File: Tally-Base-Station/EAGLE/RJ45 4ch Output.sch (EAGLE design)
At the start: 9 parts, among them J1 CAMOUT1, J2 CAMOUT2, J3 CAMOUT3, J4 CAMOUT4

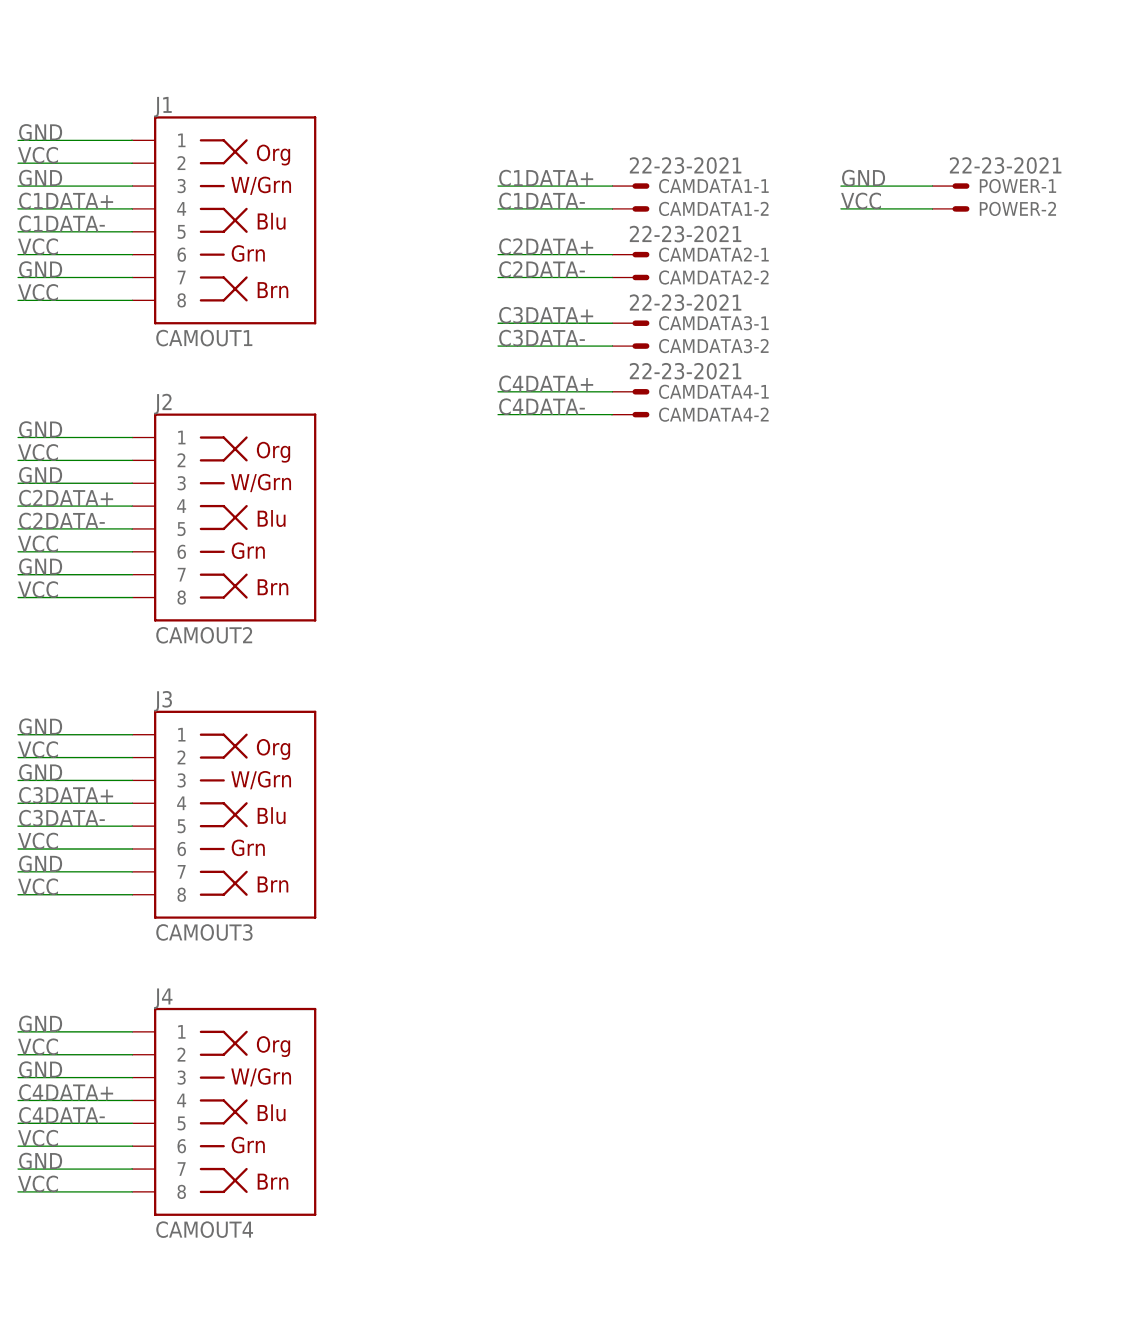
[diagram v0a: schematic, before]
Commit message: Standardize RS485 pinouts, update RJ45 pinouts.
Fix pin assignments for the RS485 interconnects to standardize on pin1 = data-.
Update the RJ45 breakouts to be mostly pin compatible with DMX over ethernet wiring standard (using pin 5/6 for V+)
Create an XLR RS485 breakout option for wiring cameras together using 3pin DMX cables
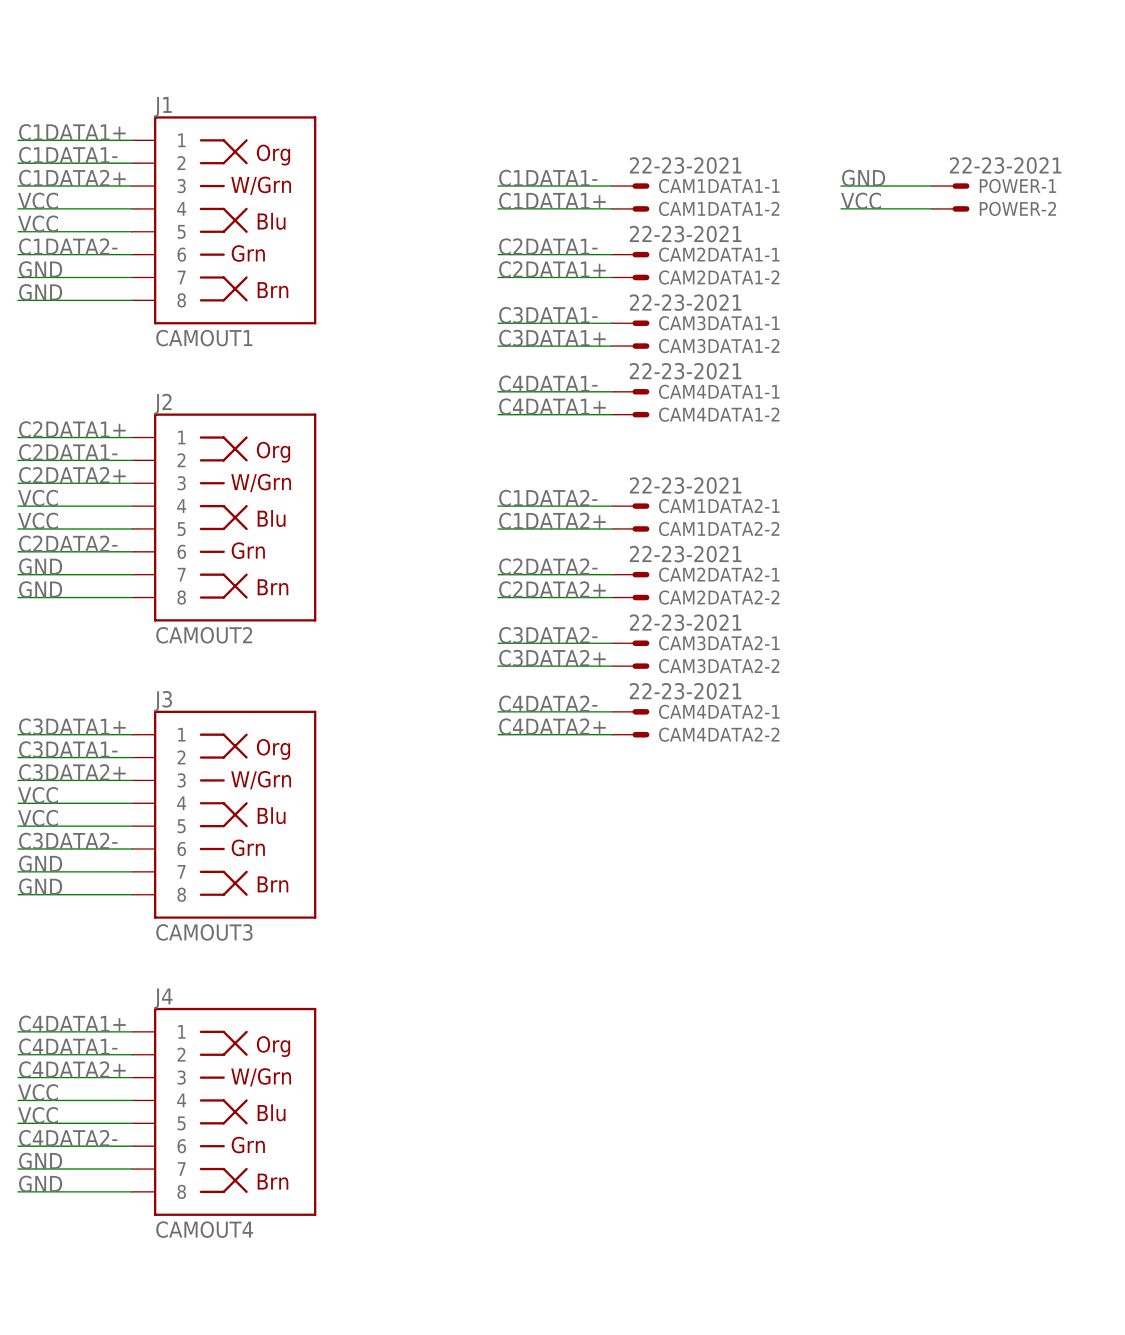
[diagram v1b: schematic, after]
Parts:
- added CAM1DATA2, CAM2DATA2, CAM3DATA2, CAM4DATA2: 22-23-2021, con-molex:22-23-2021
- renumbered CAMDATA1 to CAM1DATA1, CAMDATA2 to CAM2DATA1, CAMDATA3 to CAM3DATA1, CAMDATA4 to CAM4DATA1
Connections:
- removed net C1DATA+: CAM1DATA1-1.S, J1.4
- removed net C1DATA-: CAM1DATA1-2.S, J1.5
- removed net C2DATA+: CAM2DATA1-1.S, J2.4
- removed net C2DATA-: CAM2DATA1-2.S, J2.5
- removed net C3DATA+: CAM3DATA1-1.S, J3.4
- removed net C3DATA-: CAM3DATA1-2.S, J3.5
- removed net C4DATA+: CAM4DATA1-1.S, J4.4
- removed net C4DATA-: CAM4DATA1-2.S, J4.5
- new net C1DATA1+: CAM1DATA1-2.S, J1.1
- new net C1DATA1-: CAM1DATA1-1.S, J1.2
- new net C1DATA2+: CAM1DATA2-2.S, J1.3
- new net C1DATA2-: CAM1DATA2-1.S, J1.6
- new net C2DATA1+: CAM2DATA1-2.S, J2.1
- new net C2DATA1-: CAM2DATA1-1.S, J2.2
- new net C2DATA2+: CAM2DATA2-2.S, J2.3
- new net C2DATA2-: CAM2DATA2-1.S, J2.6
- new net C3DATA1+: CAM3DATA1-2.S, J3.1
- new net C3DATA1-: CAM3DATA1-1.S, J3.2
- new net C3DATA2+: CAM3DATA2-2.S, J3.3
- new net C3DATA2-: CAM3DATA2-1.S, J3.6
- new net C4DATA1+: CAM4DATA1-2.S, J4.1
- new net C4DATA1-: CAM4DATA1-1.S, J4.2
- new net C4DATA2+: CAM4DATA2-2.S, J4.3
- new net C4DATA2-: CAM4DATA2-1.S, J4.6
- net GND: now also J1.8, J2.8, J3.8, J4.8; no longer J1.1, J1.3, J2.1, J2.3, J3.1, J3.3, J4.1, J4.3
- net VCC: now also J1.4, J1.5, J2.4, J2.5, J3.4, J3.5, J4.4, J4.5; no longer J1.2, J1.6, J1.8, J2.2, J2.6, J2.8, J3.2, J3.6, J3.8, J4.2, J4.6, J4.8

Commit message: Update RJ45 boards to use RJHSE Amphenol jacks
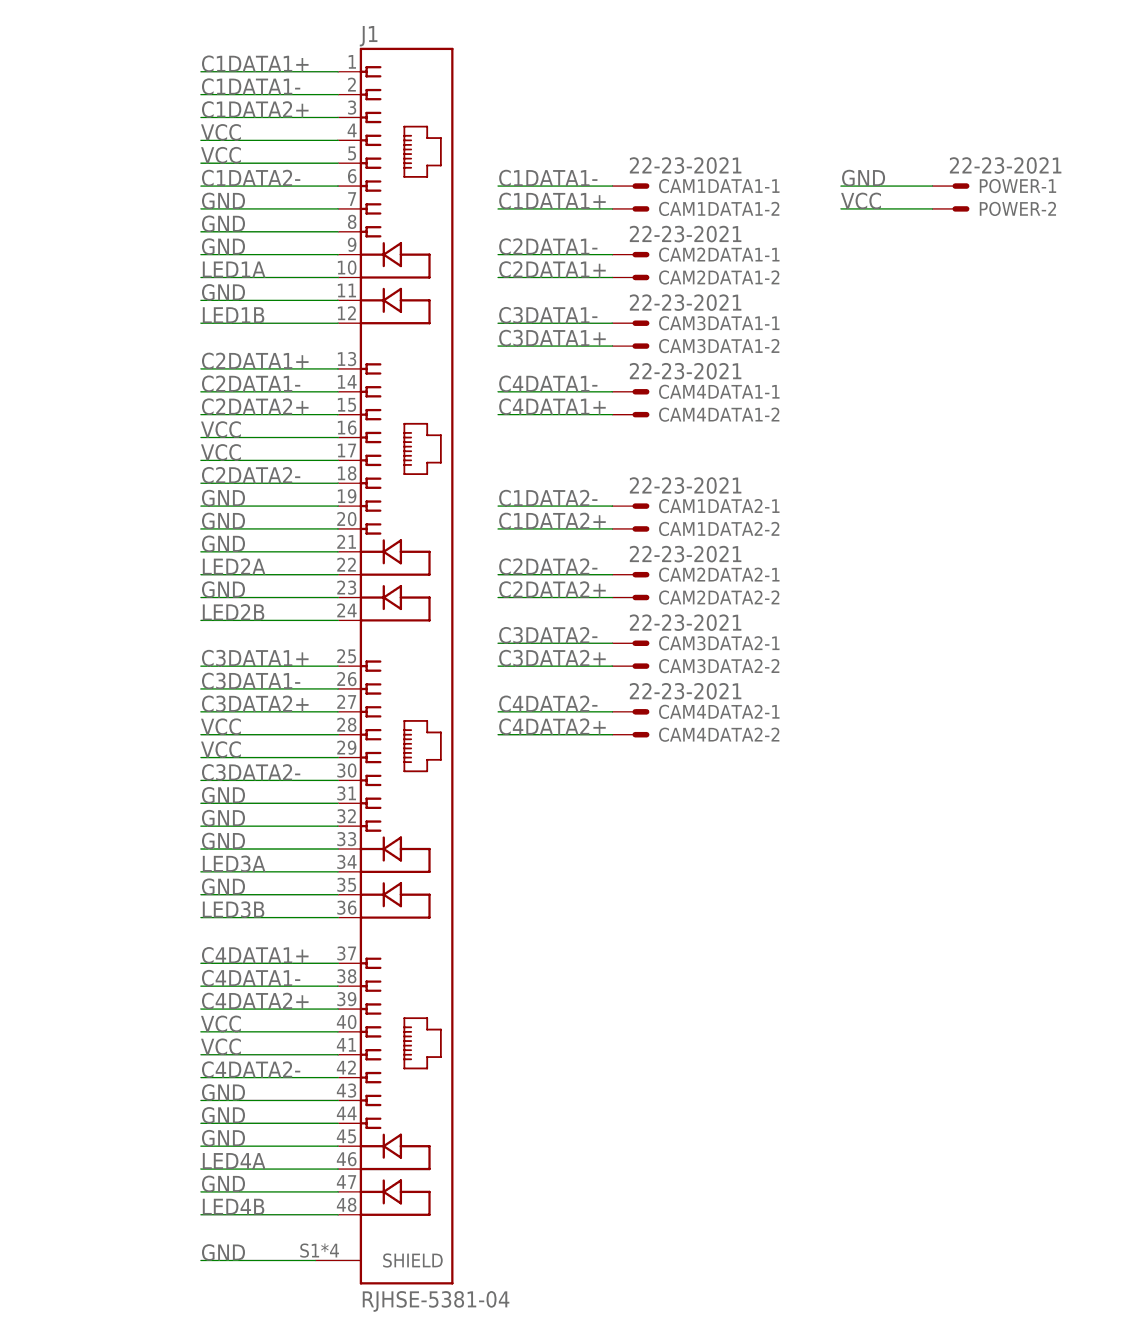
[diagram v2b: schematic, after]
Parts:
- removed J2: CAMOUT2, SparkFun-Connectors:RJ45-8
- removed J3: CAMOUT3, SparkFun-Connectors:RJ45-8
- removed J4: CAMOUT4, SparkFun-Connectors:RJ45-8
- J1: value CAMOUT1 -> RJHSE-5381-04; device SparkFun-Connectors:RJ45-8 -> RJHSE-5381-04:RJHSE-5381-04
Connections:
- new net LED1A: J1.10
- new net LED1B: J1.12
- new net LED2A: J1.22
- new net LED2B: J1.24
- new net LED3A: J1.34
- new net LED3B: J1.36
- new net LED4A: J1.46
- new net LED4B: J1.48
- net C2DATA1+: now also J1.13; no longer J2.1
- net C2DATA1-: now also J1.14; no longer J2.2
- net C2DATA2+: now also J1.15; no longer J2.3
- net C2DATA2-: now also J1.18; no longer J2.6
- net C3DATA1+: now also J1.25; no longer J3.1
- net C3DATA1-: now also J1.26; no longer J3.2
- net C3DATA2+: now also J1.27; no longer J3.3
- net C3DATA2-: now also J1.30; no longer J3.6
- net C4DATA1+: now also J1.37; no longer J4.1
- net C4DATA1-: now also J1.38; no longer J4.2
- net C4DATA2+: now also J1.39; no longer J4.3
- net C4DATA2-: now also J1.42; no longer J4.6
- net GND: now also J1.11, J1.19, J1.20, J1.21, J1.23, J1.31, J1.32, J1.33, J1.35, J1.43, J1.44, J1.45, J1.47, J1.9, J1.SHIELD; no longer J2.7, J2.8, J3.7, J3.8, J4.7, J4.8
- net VCC: now also J1.16, J1.17, J1.28, J1.29, J1.40, J1.41; no longer J2.4, J2.5, J3.4, J3.5, J4.4, J4.5
